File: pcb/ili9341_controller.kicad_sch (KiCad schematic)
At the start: 87 parts, among them J1 USB_B_Micro, J2 RP_SWD_CONN, J3 CONN_RP2040, J4 CONN_FPGA, J5 CONN_TFT, Q1 NPN, Q2 NPN, Q3 NPN, SW1 RP_RST_SW, SW2 RP_USB_BOOT_SW, U1 ICE40UP5K-SG48ITR, U2 LM3880, U3 LD1117S33TR_SOT223, U4 LD1117S12TR_SOT223, U5 LD1117S25TR_SOT223, U6 RP2040, U7 W25Q128JVS, Y1 12MHz

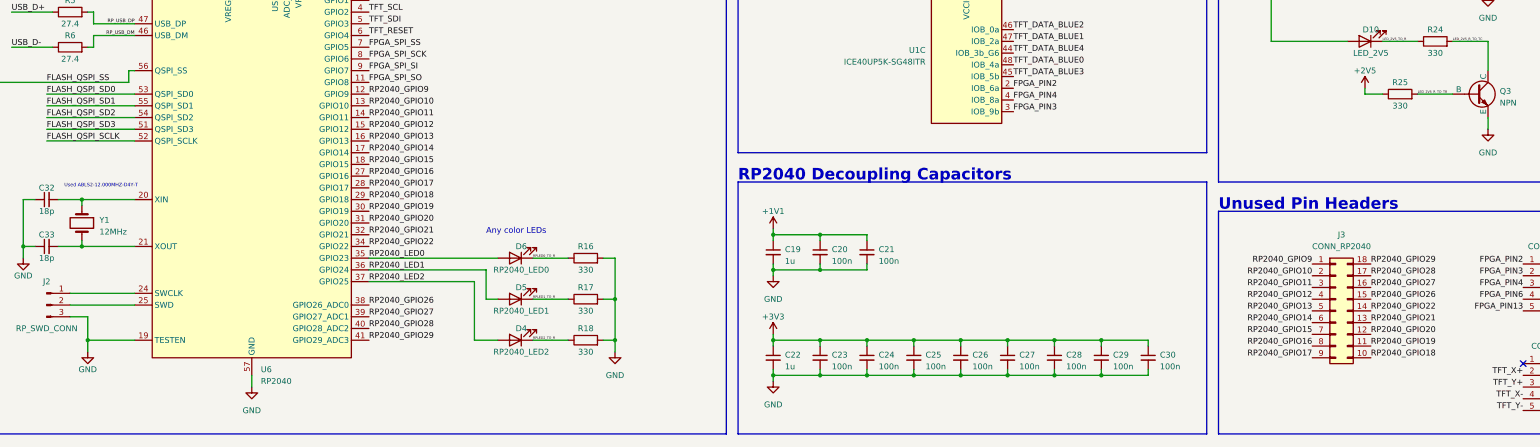
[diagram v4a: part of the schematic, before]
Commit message: fix unconnected pins
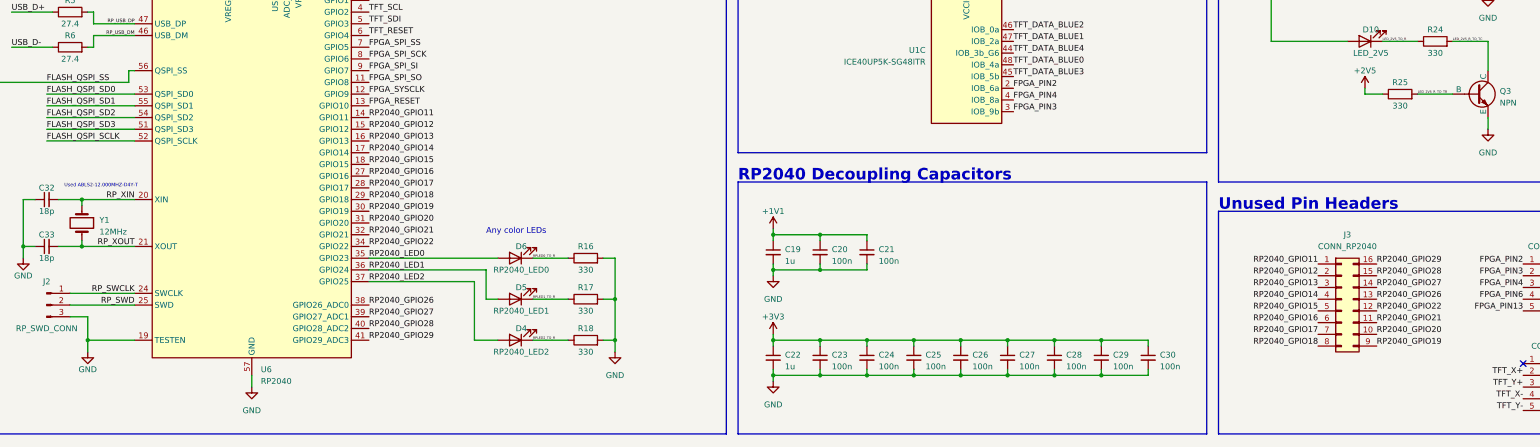
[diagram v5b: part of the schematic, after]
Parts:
- removed J3: CONN_RP2040, symbol Connector_Generic:Conn_02x09_Counter_Clockwise
- added J3: CONN_RP2040, symbol Connector_Generic:Conn_02x08_Counter_Clockwise
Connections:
- net RP2040_GPIO10 is gone; now on net FPGA_RESET: U6.13 (GPIO10)
- net RP2040_GPIO9 is gone; now on net FPGA_SYSCLK: U6.12 (GPIO9)
- net RP2040_GPIO11: now also J3.1 (Pin_1)
- net RP2040_GPIO12: now also J3.2 (Pin_2)
- net RP2040_GPIO13: now also J3.3 (Pin_3)
- net RP2040_GPIO14: now also J3.4 (Pin_4)
- net RP2040_GPIO15: now also J3.5 (Pin_5)
- net RP2040_GPIO16: now also J3.6 (Pin_6)
- net RP2040_GPIO17: now also J3.7 (Pin_7)
- net RP2040_GPIO18: now also J3.8 (Pin_8)
- net RP2040_GPIO19: now also J3.9 (Pin_9)
- net RP2040_GPIO20: now also J3.10 (Pin_10)
- net RP2040_GPIO21: now also J3.11 (Pin_11)
- net RP2040_GPIO22: now also J3.12 (Pin_12)
- net RP2040_GPIO26: now also J3.13 (Pin_13)
- net RP2040_GPIO27: now also J3.14 (Pin_14)
- net RP2040_GPIO28: now also J3.15 (Pin_15)
- net RP2040_GPIO29: now also J3.16 (Pin_16)
- net RP_XIN: now reaches C32.2, U6.20 (XIN), Y1.1
- net RP_XOUT: now reaches C33.2, U6.21 (XOUT), Y1.2
- net RP_SWCLK: now reaches J2.1 (Pin_1), U6.24 (SWCLK)
- net RP_SWD: now reaches J2.2 (Pin_2), U6.25 (SWD)
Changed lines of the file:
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@@
     (effects (font (size 1.27 1.27)) (justify left bottom))
   )
-  (label "RP2040_GPIO9" (at 138.43 245.11 0) (fields_autoplaced)
-    (effects (font (size 1.27 1.27)) (justify left bottom))
-  )
   (label "TFT_DATA_RED2" (at 259.08 68.58 0) (fields_autoplaced)
     (effects (font (size 1.27 1.27)) (justify left bottom))
@@
     (effects (font (size 1.27 1.27)) (justify left bottom))
   )
-  (label "RP2040_GPIO12" (at 342.9 289.56 180) (fields_autoplaced)
+  (label "RP2040_GPIO12" (at 344.17 284.48 180) (fields_autoplaced)
+    (effects (font (size 1.27 1.27)) (justify right bottom))
+  )
+  (label "RP_SWD" (at 87.63 290.83 180) (fields_autoplaced)
     (effects (font (size 1.27 1.27)) (justify right bottom))
   )
@@
     (effects (font (size 0.5 0.5)) (justify left bottom))
   )
-  (label "RP2040_GPIO17" (at 342.9 302.26 180) (fields_autoplaced)
-    (effects (font (size 1.27 1.27)) (justify right bottom))
-  )
-  (label "RP2040_GPIO9" (at 342.9 281.94 180) (fields_autoplaced)
+  (label "RP2040_GPIO17" (at 344.17 297.18 180) (fields_autoplaced)
     (effects (font (size 1.27 1.27)) (justify right bottom))
   )
@@
     (effects (font (size 0.75 0.75)) (justify right bottom))
   )
-  (label "RP2040_GPIO10" (at 342.9 284.48 180) (fields_autoplaced)
-    (effects (font (size 1.27 1.27)) (justify right bottom))
-  )
   (label "LED_2V5_R_TO_TC" (at 373.38 233.68 0) (fields_autoplaced)
     (effects (font (size 0.5 0.5)) (justify left bottom))
   )
-  (label "RP2040_GPIO27" (at 355.6 287.02 0) (fields_autoplaced)
+  (label "RP2040_GPIO27" (at 356.87 287.02 0) (fields_autoplaced)
     (effects (font (size 1.27 1.27)) (justify left bottom))
   )
@@
     (effects (font (size 1.27 1.27)) (justify left bottom))
   )
-  (label "RP2040_GPIO13" (at 138.43 255.27 0) (fields_autoplaced)
+  (label "FPGA_SYSCLK" (at 138.43 245.11 0) (fields_autoplaced)
     (effects (font (size 1.27 1.27)) (justify left bottom))
   )
-  (label "RP2040_GPIO18" (at 355.6 302.26 0) (fields_autoplaced)
+  (label "RP2040_GPIO13" (at 138.43 255.27 0) (fields_autoplaced)
     (effects (font (size 1.27 1.27)) (justify left bottom))
   )
+  (label "RP2040_GPIO18" (at 344.17 299.72 180) (fields_autoplaced)
+    (effects (font (size 1.27 1.27)) (justify right bottom))
+  )
   (label "TFT_DATA_BLUE3" (at 405.13 96.52 0) (fields_autoplaced)
     (effects (font (size 1.27 1.27)) (justify left bottom))
@@
     (effects (font (size 1.27 1.27)) (justify left bottom))
   )
-  (label "RP2040_GPIO15" (at 342.9 297.18 180) (fields_autoplaced)
+  (label "RP2040_GPIO15" (at 344.17 292.1 180) (fields_autoplaced)
     (effects (font (size 1.27 1.27)) (justify right bottom))
   )
@@
     (effects (font (size 1.27 1.27)) (justify right bottom))
   )
-  (label "RP2040_GPIO20" (at 355.6 297.18 0) (fields_autoplaced)
+  (label "RP2040_GPIO20" (at 356.87 297.18 0) (fields_autoplaced)
     (effects (font (size 1.27 1.27)) (justify left bottom))
   )
-  (label "RP2040_GPIO13" (at 342.9 292.1 180) (fields_autoplaced)
+  (label "RP_SWCLK" (at 87.63 288.29 180) (fields_autoplaced)
     (effects (font (size 1.27 1.27)) (justify right bottom))
   )
-  (label "RP2040_GPIO11" (at 342.9 287.02 180) (fields_autoplaced)
+  (label "RP2040_GPIO13" (at 344.17 287.02 180) (fields_autoplaced)
+    (effects (font (size 1.27 1.27)) (justify right bottom))
+  )
+  (label "RP2040_GPIO11" (at 344.17 281.94 180) (fields_autoplaced)
     (effects (font (size 1.27 1.27)) (justify right bottom))
   )
@@
     (effects (font (size 0.75 0.75)) (justify right bottom))
   )
-  (label "RP2040_GPIO14" (at 342.9 294.64 180) (fields_autoplaced)
+  (label "RP2040_GPIO14" (at 344.17 289.56 180) (fields_autoplaced)
     (effects (font (size 1.27 1.27)) (justify right bottom))
   )
@@
     (effects (font (size 1.27 1.27)) (justify right bottom))
   )
+  (label "RP_XOUT" (at 87.63 278.13 180) (fields_autoplaced)
+    (effects (font (size 1.27 1.27)) (justify right bottom))
+  )
   (label "LED_3V3_TO_R" (at 358.14 204.47 0) (fields_autoplaced)
     (effects (font (size 0.5 0.5)) (justify left bottom))
   )
-  (label "RP2040_GPIO16" (at 342.9 299.72 180) (fields_autoplaced)
+  (label "RP2040_GPIO16" (at 344.17 294.64 180) (fields_autoplaced)
     (effects (font (size 1.27 1.27)) (justify right bottom))
   )
@@
     (effects (font (size 1.27 1.27)) (justify left bottom))
   )
-  (label "RP2040_GPIO26" (at 355.6 289.56 0) (fields_autoplaced)
+  (label "RP2040_GPIO26" (at 356.87 289.56 0) (fields_autoplaced)
     (effects (font (size 1.27 1.27)) (justify left bottom))
   )
@@
     (effects (font (size 1.27 1.27)) (justify left bottom))
   )
+  (label "RP_XIN" (at 87.63 267.97 180) (fields_autoplaced)
+    (effects (font (size 1.27 1.27)) (justify right bottom))
+  )
   (label "TFT_DATA_BLUE0" (at 278.13 238.76 0) (fields_autoplaced)
     (effects (font (size 1.27 1.27)) (justify left bottom))
@@
     (effects (font (size 1.27 1.27)) (justify left bottom))
   )
-  (label "RP2040_GPIO29" (at 355.6 281.94 0) (fields_autoplaced)
+  (label "RP2040_GPIO29" (at 356.87 281.94 0) (fields_autoplaced)
     (effects (font (size 1.27 1.27)) (justify left bottom))
   )
@@
     (effects (font (size 0.5 0.5)) (justify left bottom))
   )
+  (label "FPGA_RESET" (at 138.43 247.65 0) (fields_autoplaced)
+    (effects (font (size 1.27 1.27)) (justify left bottom))
+  )
   (label "FPGA_SPI_SS" (at 138.43 234.95 0) (fields_autoplaced)
     (effects (font (size 1.27 1.27)) (justify left bottom))
@@
     (effects (font (size 1.27 1.27)) (justify left bottom))
   )
-  (label "RP2040_GPIO21" (at 355.6 294.64 0) (fields_autoplaced)
+  (label "RP2040_GPIO21" (at 356.87 294.64 0) (fields_autoplaced)
     (effects (font (size 1.27 1.27)) (justify left bottom))
   )
@@
     (effects (font (size 1.27 1.27)) (justify right bottom))
   )
-  (label "RP2040_GPIO19" (at 355.6 299.72 0) (fields_autoplaced)
+  (label "RP2040_GPIO19" (at 356.87 299.72 0) (fields_autoplaced)
     (effects (font (size 1.27 1.27)) (justify left bottom))
   )
@@
     (effects (font (size 1.27 1.27)) (justify left bottom))
   )
-  (label "RP2040_GPIO28" (at 355.6 284.48 0) (fields_autoplaced)
+  (label "RP2040_GPIO28" (at 356.87 284.48 0) (fields_autoplaced)
     (effects (font (size 1.27 1.27)) (justify left bottom))
   )
-  (label "RP2040_GPIO22" (at 355.6 292.1 0) (fields_autoplaced)
+  (label "RP2040_GPIO22" (at 356.87 292.1 0) (fields_autoplaced)
     (effects (font (size 1.27 1.27)) (justify left bottom))
   )
@@
     (effects (font (size 1.27 1.27)) (justify left bottom))
   )
-  (label "RP2040_GPIO10" (at 138.43 247.65 0) (fields_autoplaced)
-    (effects (font (size 1.27 1.27)) (justify left bottom))
-  )
   (label "FLASH_QSPI_SS" (at 68.58 242.57 0) (fields_autoplaced)
     (effects (font (size 1.27 1.27)) (justify left bottom))
@@
     )
   )
-  (symbol (lib_id "Connector_Generic:Conn_02x09_Counter_Clockwise") (at 347.98 292.1 0) (unit 1)
-    (in_bom yes) (on_board yes) (dnp no)
-    (property "Reference" "J3" (at 349.25 275.59 0)
-      (effects (font (size 1.27 1.27)))
-    )
-    (property "Value" "CONN_RP2040" (at 349.25 278.13 0)
-      (effects (font (size 1.27 1.27)))
-    )
-    (property "Footprint" "" (at 347.98 292.1 0)
-      (effects (font (size 1.27 1.27)) hide)
-    )
-    (property "Datasheet" "~" (at 347.98 292.1 0)
-      (effects (font (size 1.27 1.27)) hide)
-    )
-    (pin "1")
-    (pin "10")
-    (pin "11")
-    (pin "12")
-    (pin "13")
-    (pin "14")
-    (pin "15")
-    (pin "16")
-    (pin "17")
-    (pin "18")
-    (pin "2")
-    (pin "3")
-    (pin "4")
-    (pin "5")
-    (pin "6")
-    (pin "7")
-    (pin "8")
-    (pin "9")
-    (instances
-      (project "ili9341_controller"
-        (path "/5ab5cbe5-2e2b-40a8-992c-b266cf7668f6"
-          (reference "J3") (unit 1)
-        )
-      )
-    )
-  )
   (symbol (lib_id "Device:C_Small") (at 128.27 138.43 0) (unit 1)
     (in_bom yes) (on_board yes) (dnp no) (fields_autoplaced)
@@
         )
       )
+    )
+  )
+  (symbol (lib_id "Connector_Generic:Conn_02x08_Counter_Clockwise") (at 349.25 289.56 0) (unit 1)
+    (in_bom yes) (on_board yes) (dnp no)
+    (property "Reference" "J3" (at 350.52 275.59 0)
+      (effects (font (size 1.27 1.27)))
+    )
+    (property "Value" "CONN_RP2040" (at 350.52 278.13 0)
+      (effects (font (size 1.27 1.27)))
+    )
+    (property "Footprint" "" (at 349.25 289.56 0)
+      (effects (font (size 1.27 1.27)) hide)
+    )
+    (property "Datasheet" "~" (at 349.25 289.56 0)
+      (effects (font (size 1.27 1.27)) hide)
+    )
+    (pin "1")
+    (pin "10")
+    (pin "11")
+    (pin "12")
+    (pin "13")
+    (pin "14")
+    (pin "15")
+    (pin "16")
+    (pin "2")
+    (pin "3")
+    (pin "4")
+    (pin "5")
+    (pin "6")
+    (pin "7")
+    (pin "8")
+    (pin "9")
+    (instances
+      (project "ili9341_controller"
+        (path "/5ab5cbe5-2e2b-40a8-992c-b266cf7668f6"
+          (reference "J3") (unit 1)
+        )
+      )

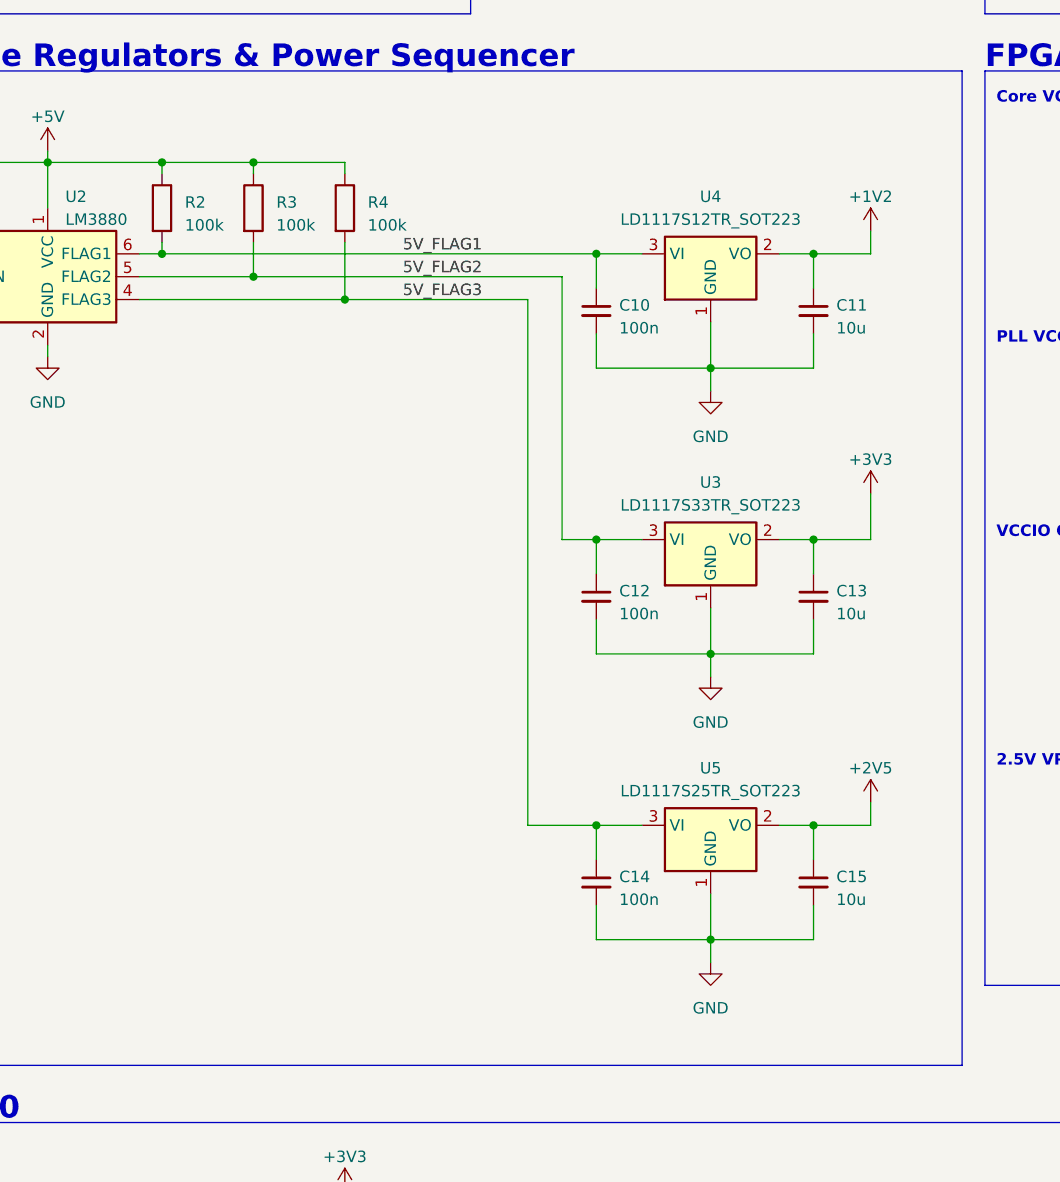
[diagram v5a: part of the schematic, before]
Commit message: switch to use TLV755P linear regulators
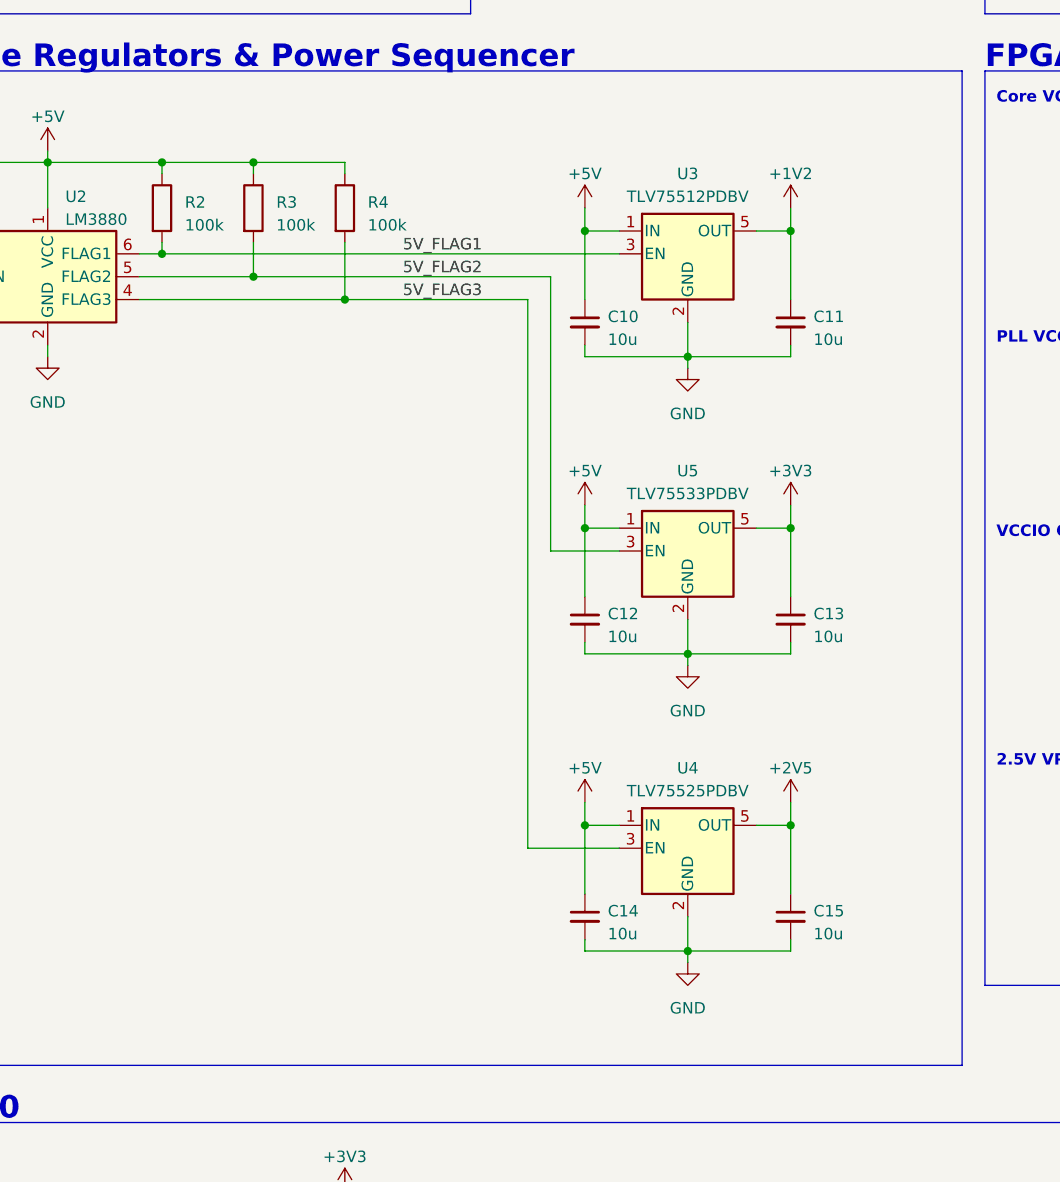
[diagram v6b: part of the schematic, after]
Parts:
- removed U3: LD1117S33TR_SOT223, Package_TO_SOT_SMD:SOT-223-3_TabPin2, symbol Regulator_Linear:LD1117S33TR_SOT223
- removed U4: LD1117S12TR_SOT223, Package_TO_SOT_SMD:SOT-223-3_TabPin2, symbol Regulator_Linear:LD1117S12TR_SOT223
- removed U5: LD1117S25TR_SOT223, Package_TO_SOT_SMD:SOT-223-3_TabPin2, symbol Regulator_Linear:LD1117S25TR_SOT223
- added U3: TLV75512PDBV, Package_TO_SOT_SMD:SOT-23-5, symbol Regulator_Linear:TLV75512PDBV
- added U4: TLV75525PDBV, Package_TO_SOT_SMD:SOT-23-5, symbol Regulator_Linear:TLV75525PDBV
- added U5: TLV75533PDBV, Package_TO_SOT_SMD:SOT-23-5, symbol Regulator_Linear:TLV75533PDBV
- C10, C12, C14: value 100n -> 10u
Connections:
- net +1V2: now also U3.5 (OUT)
- net +2V5: now also U4.5 (OUT)
- net +3V3: now also U5.5 (OUT)
- net +5V: now also C10.1, C12.1, C14.1, U3.1 (IN), U4.1 (IN), U5.1 (IN)
- net 5V_FLAG1: now also U3.3 (EN); no longer C10.1
- net 5V_FLAG2: now also U5.3 (EN); no longer C12.1
- net 5V_FLAG3: now also U4.3 (EN); no longer C14.1
- net GND: now also U3.2 (GND), U4.2 (GND), U5.2 (GND)
